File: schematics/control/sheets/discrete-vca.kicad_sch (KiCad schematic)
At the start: 19 parts, among them Q3 2N3904, Q4 2N3904, U11 TL072, U12 LM13700

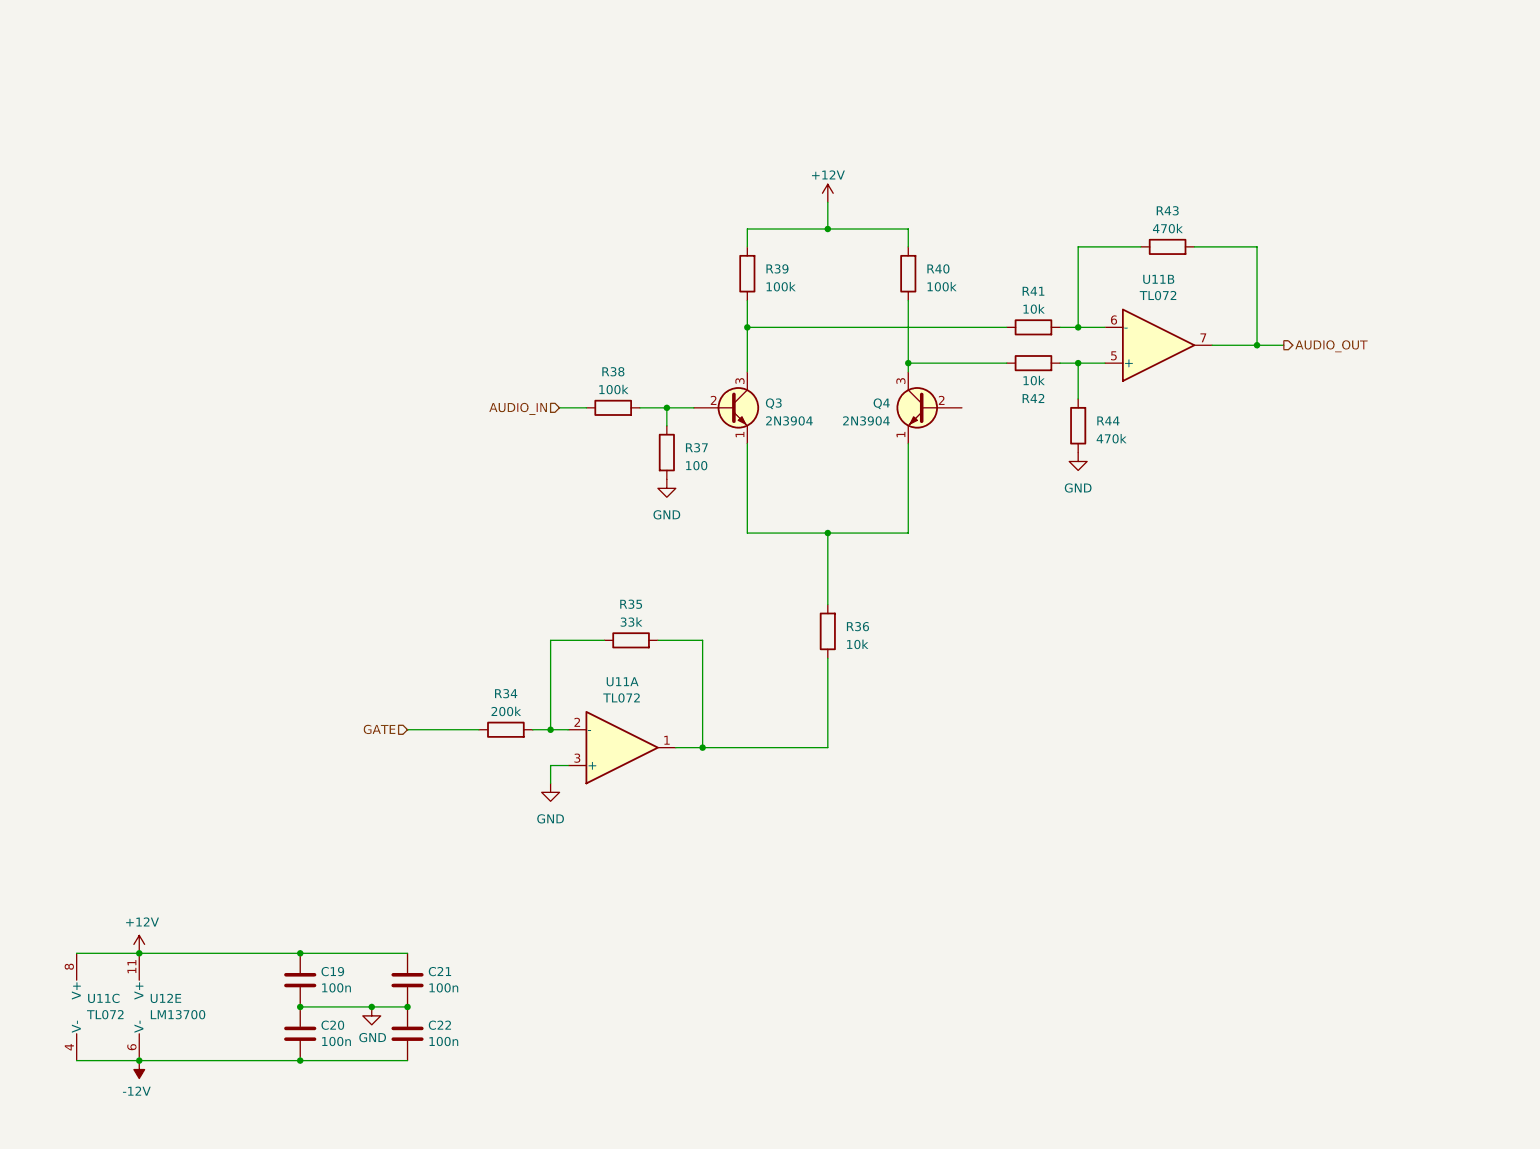
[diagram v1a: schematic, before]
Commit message: Added pulse width mod schematics
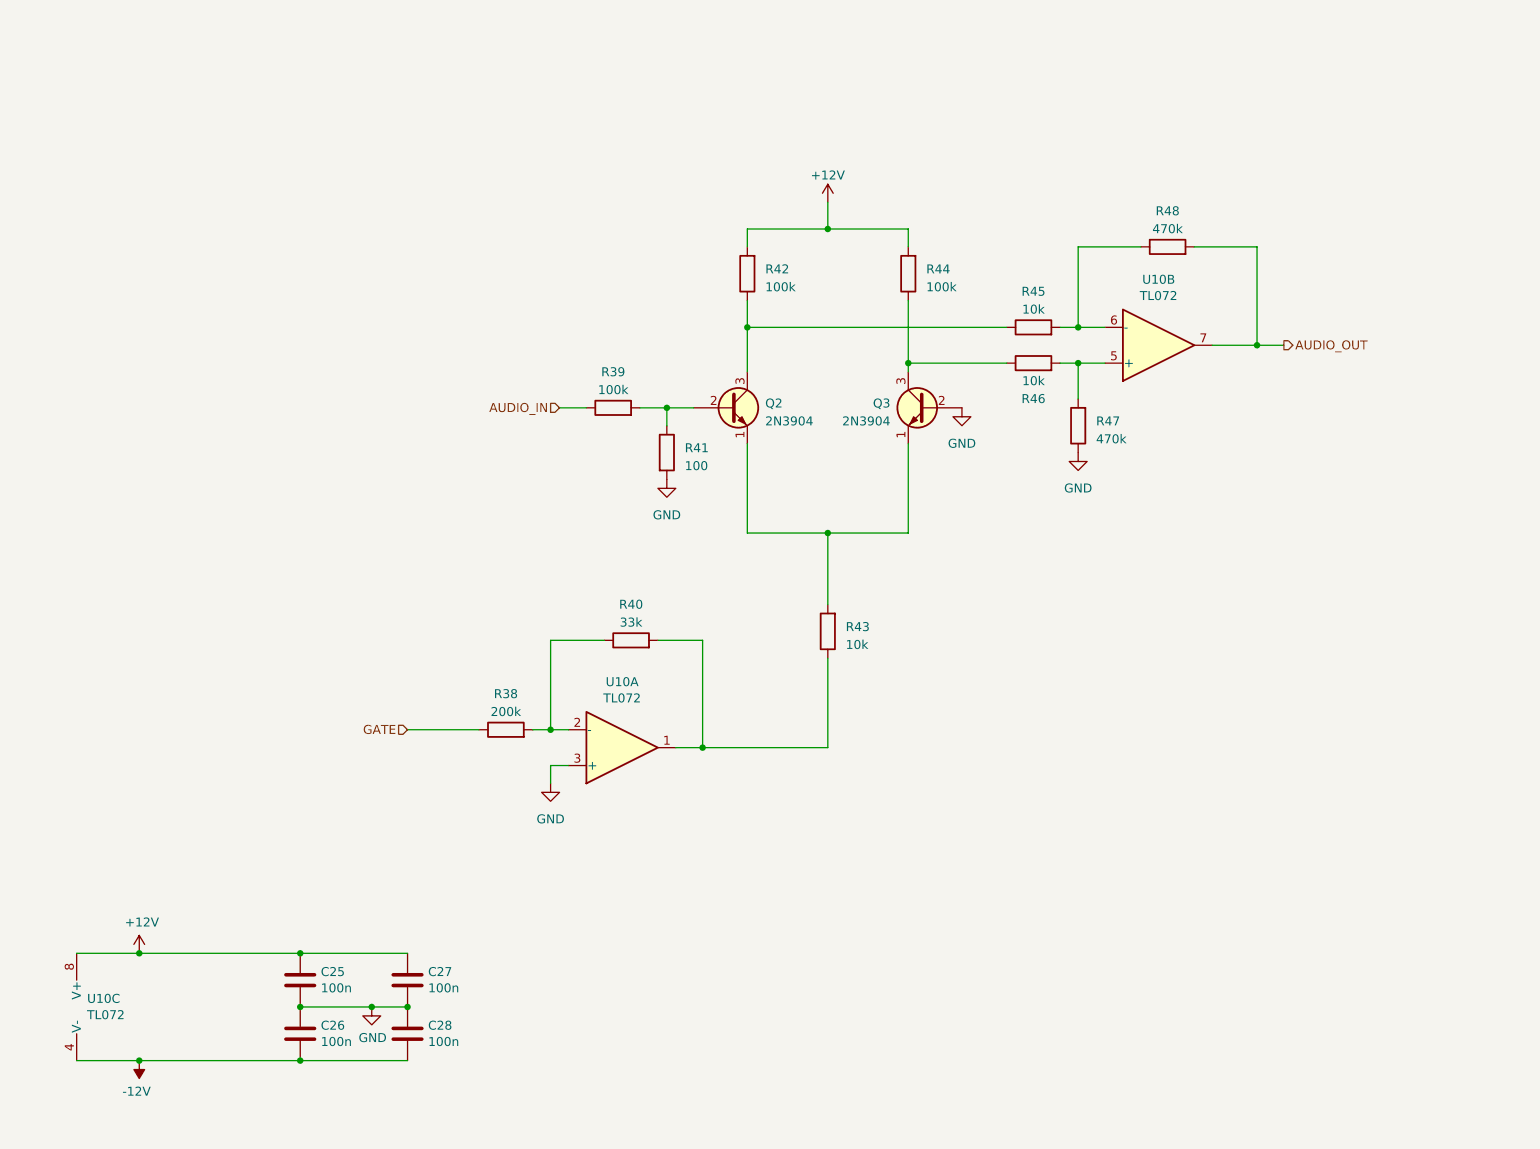
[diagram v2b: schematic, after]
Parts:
- removed U12: LM13700, Package_DIP:DIP-16_W7.62mm, symbol Amplifier_Operational:LM13700
- renumbered C19 to C25, C20 to C26, C21 to C27, C22 to C28, Q3 to Q2, Q4 to Q3, R34 to R38, R38 to R39, R35 to R40, R37 to R41, R39 to R42, R36 to R43, R40 to R44, R41 to R45, R42 to R46, R44 to R47, R43 to R48, U11 to U10
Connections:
- net GND: now also Q3.2 (B)

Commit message: Updated VCA
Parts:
- removed C25, C26, C27, C28: 100n, Capacitor_THT:C_Disc_D3.0mm_W2.0mm_P2.50mm, symbol Device:C
- removed Q2, Q3: 2N3904, Package_TO_SOT_THT_AKL:TO-92_Inline_Wide_EBC, symbol PCM_Transistor_BJT_AKL:2N3904
- removed R46: 10k, symbol Device:R
- removed U10: TL072, Package_DIP:DIP-8_W7.62mm, symbol Amplifier_Operational:TL072
- added Q2, Q3, Q4, Q5: BC548, Package_TO_SOT_THT_AKL:TO-92_Inline_Wide_CBE, symbol PCM_Transistor_BJT_AKL:BC548
- added Q6: BC558, Package_TO_SOT_THT_AKL:TO-92_Inline_Wide_CBE, symbol PCM_Transistor_BJT_AKL:BC558
- added R57: 470, symbol Device:R
- added RV_BIAS1: 100k, symbol Device:R_Potentiometer_Trim
- added RV_REJECTION1: 10k, symbol Device:R_Potentiometer_Trim
- added TP_VCA_AU_IN1, TP_VCA_GATE1, TP_VCA_OUT1: TestPoint, symbol Connector:TestPoint
- added U6: TL072, Package_DIP:DIP-8_W7.62mm, symbol Amplifier_Operational:TL072
- R38: value 200k -> 22k
- R40: value 33k -> 22k
- R41: value 100 -> 470
- R42, R44: value 100k -> 4.7k
- R43, R45: value 10k -> 100k
- R47, R48: value 470k -> 33k
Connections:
- net +12V: now also R43.1, RV_REJECTION1.2; no longer R42.2, R44.2
- net -12V: now also R45.2, Q4.3 (E), Q5.3 (E)
- net AUDIO_OUT: now also TP_VCA_OUT1.1, U6.1
- net GATE: now also R40.1; no longer R38.1
- net GND: now also Q6.2 (B), R57.2
- net at R40.2: now also R38.2, Q6.3 (E), TP_VCA_GATE1.1; no longer R43.1
- net at R43.2: now also RV_BIAS1.1
- net at R47.2: now also R44.1, Q3.1 (C), U6.3 (+)
- net at R39.2, R41.1: now also Q2.2 (B), TP_VCA_AU_IN1.1
- net at R42.1: now also R48.1, Q2.1 (C), U6.2 (-); no longer R45.1
- new net: Q2.3 (E), Q3.3 (E), Q4.1 (C)
- new net: R42.2, RV_REJECTION1.1
- new net: R44.2, RV_REJECTION1.3
- new net: R38.1, RV_BIAS1.2
- new net: R45.1, RV_BIAS1.3
- new net: Q4.2 (B), Q5.1 (C), Q5.2 (B), Q6.1 (C)
- new net: Q3.2 (B), R57.1
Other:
- note added: "Calibration: - Connect audio on the input - Set RV_BIAS1 until you just can't hear anything on the output - Use RV_REJECTION1 to compensate DC offset if there's any."
- note added: "Max CV input voltage 5-12V"
- note added: "References: https://kassu2000.blogspot.com/2015/10/vca.html https://www.schmitzbits.de/vca.html"
- company: (none) -> Shmøergh
- title: (none) -> Discrete linear VCA
- moved on the sheet: R39, R41, R42, R44, R47, R48

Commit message: Added all UI components to schematics
- digital UI
- filter UI
- updated voice interface connection
- simplified schematics a lot
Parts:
- added RV_GATE_DAMP1: 100k, symbol Device:R_Potentiometer_Trim
- Q2: renamed from Q6; footprint Package_TO_SOT_THT_AKL:TO-92_Inline_Wide_CBE -> (none)
- Q3: renamed from Q5; footprint Package_TO_SOT_THT_AKL:TO-92_Inline_Wide_CBE -> (none)
- Q4: renamed from Q2; footprint Package_TO_SOT_THT_AKL:TO-92_Inline_Wide_CBE -> (none)
- Q5: renamed from Q4; footprint Package_TO_SOT_THT_AKL:TO-92_Inline_Wide_CBE -> (none)
- Q6: renamed from Q3; footprint Package_TO_SOT_THT_AKL:TO-92_Inline_Wide_CBE -> (none)
- U?: renamed from U6; footprint Package_DIP:DIP-8_W7.62mm -> (none)
- renumbered R43 to R49, R45 to R50, R40 to R51, R38 to R52, R39 to R53, R41 to R54, R42 to R55, R44 to R56, R47 to R58, R48 to R59
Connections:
- net GATE: now also RV_GATE_DAMP1.1; no longer R51.1
- net GND: now also RV_GATE_DAMP1.3
- new net: R51.1, RV_GATE_DAMP1.2

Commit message: Schemo work
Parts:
- Q2, Q3, Q4, Q5, Q6: footprint (none) -> PCM_Package_TO_SOT_THT_AKL:TO-92_Inline_Wide
- R49, R50, R51, R52, R53, R54, R55, R56, R57, R58, R59: footprint (none) -> Shmoergh_Custom_Footprints:R_Axial_DIN0207_L6.3mm_D2.5mm_P7.62mm_Horizontal
- RV_GATE_DAMP1: footprint (none) -> Potentiometer_THT:Potentiometer_Runtron_RM-065_Vertical
- RV_REJECTION1: footprint (none) -> Potentiometer_THT:Potentiometer_Bourns_3296W_Vertical
- RV_VCA_BIAS1: renamed from RV_BIAS1; footprint (none) -> Potentiometer_THT:Potentiometer_Runtron_RM-065_Vertical
- TP_VCA_AU_IN1, TP_VCA_GATE1, TP_VCA_OUT1: footprint (none) -> TestPoint:TestPoint_THTPad_D2.0mm_Drill1.0mm
- U?: footprint (none) -> PCM_Package_DIP_AKL:DIP-8_W7.62mm_LongPads
